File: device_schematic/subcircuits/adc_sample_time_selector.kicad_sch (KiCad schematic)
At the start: 3 parts, among them SW1 ADC speed switch

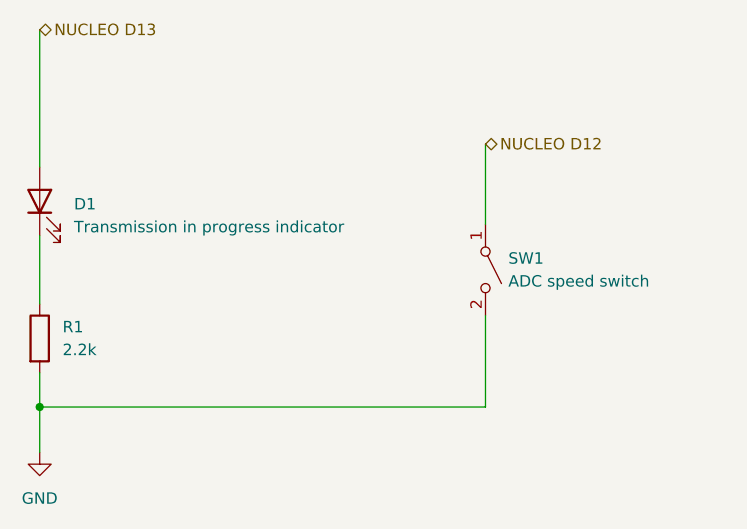
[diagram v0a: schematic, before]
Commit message: Device schematic finished version
+ correction to use D7 in place of D13
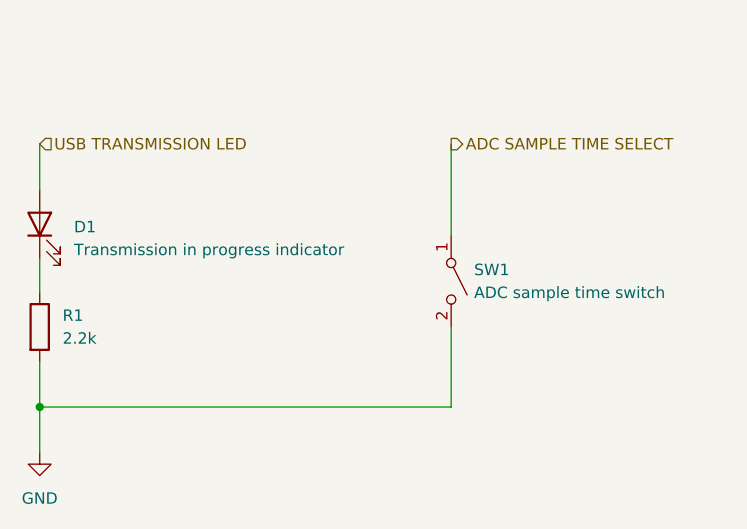
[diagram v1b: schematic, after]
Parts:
- SW1: value ADC speed switch -> ADC sample time switch
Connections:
- net NUCLEO D12 renamed ADC SAMPLE TIME SELECT
- net NUCLEO D13 renamed USB TRANSMISSION LED
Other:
- moved on the sheet: D1, R1, SW1
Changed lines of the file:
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@@
   (junction (at 110.49 119.38) (diameter 0) (color 0 0 0 0)
   )
-  (wire (pts (xy 110.49 119.38) (xy 160.02 119.38))
+  (wire (pts (xy 110.49 119.38) (xy 156.21 119.38))
     (stroke (width 0) (type default) (color 0 0 0 0))
   )
-  (wire (pts (xy 110.49 100.33) (xy 110.49 107.95))
+  (wire (pts (xy 110.49 102.87) (xy 110.49 106.68))
     (stroke (width 0) (type default) (color 0 0 0 0))
   )
-  (wire (pts (xy 160.02 90.17) (xy 160.02 99.06))
+  (wire (pts (xy 156.21 90.17) (xy 156.21 100.33))
     (stroke (width 0) (type default) (color 0 0 0 0))
   )
-  (wire (pts (xy 160.02 109.22) (xy 160.02 119.38))
+  (wire (pts (xy 156.21 110.49) (xy 156.21 119.38))
     (stroke (width 0) (type default) (color 0 0 0 0))
   )
-  (wire (pts (xy 110.49 77.47) (xy 110.49 92.71))
+  (wire (pts (xy 110.49 90.17) (xy 110.49 95.25))
     (stroke (width 0) (type default) (color 0 0 0 0))
   )
-  (wire (pts (xy 110.49 115.57) (xy 110.49 119.38))
+  (wire (pts (xy 110.49 114.3) (xy 110.49 119.38))
     (stroke (width 0) (type default) (color 0 0 0 0))
   )
@@
     (stroke (width 0) (type default) (color 0 0 0 0))
   )
-  (hierarchical_label "NUCLEO D13" (shape bidirectional) (at 110.49 77.47 0)
+  (hierarchical_label "USB TRANSMISSION LED" (shape input) (at 110.49 90.17 0)
     (effects (font (size 1.27 1.27)) (justify left))
   )
-  (hierarchical_label "NUCLEO D12" (shape bidirectional) (at 160.02 90.17 0)
+  (hierarchical_label "ADC SAMPLE TIME SELECT" (shape output) (at 156.21 90.17 0)
     (effects (font (size 1.27 1.27)) (justify left))
   )
-  (symbol (lib_id "Device:R") (at 110.49 111.76 0) (unit 1)
+  (symbol (lib_id "Device:R") (at 110.49 110.49 0) (unit 1)
     (in_bom yes) (on_board yes) (fields_autoplaced)
-    (property "Reference" "R1" (id 0) (at 113.03 110.4899 0)
+    (property "Reference" "R1" (id 0) (at 113.03 109.2199 0)
       (effects (font (size 1.27 1.27)) (justify left))
     )
-    (property "Value" "2.2k" (id 1) (at 113.03 113.0299 0)
+    (property "Value" "2.2k" (id 1) (at 113.03 111.7599 0)
       (effects (font (size 1.27 1.27)) (justify left))
     )
-    (property "Footprint" "" (id 2) (at 108.712 111.76 90)
+    (property "Footprint" "" (id 2) (at 108.712 110.49 90)
       (effects (font (size 1.27 1.27)) hide)
     )
-    (property "Datasheet" "~" (id 3) (at 110.49 111.76 0)
+    (property "Datasheet" "~" (id 3) (at 110.49 110.49 0)
       (effects (font (size 1.27 1.27)) hide)
     )
@@
     (pin "1")
   )
-  (symbol (lib_id "Device:LED") (at 110.49 96.52 90) (unit 1)
+  (symbol (lib_id "Device:LED") (at 110.49 99.06 90) (unit 1)
     (in_bom yes) (on_board yes) (fields_autoplaced)
-    (property "Reference" "D1" (id 0) (at 114.3 96.8374 90)
+    (property "Reference" "D1" (id 0) (at 114.3 99.3774 90)
       (effects (font (size 1.27 1.27)) (justify right))
     )
-    (property "Value" "Transmission in progress indicator" (id 1) (at 114.3 99.3774 90)
+    (property "Value" "Transmission in progress indicator" (id 1) (at 114.3 101.9174 90)
       (effects (font (size 1.27 1.27)) (justify right))
     )
-    (property "Footprint" "" (id 2) (at 110.49 96.52 0)
+    (property "Footprint" "" (id 2) (at 110.49 99.06 0)
       (effects (font (size 1.27 1.27)) hide)
     )
-    (property "Datasheet" "~" (id 3) (at 110.49 96.52 0)
+    (property "Datasheet" "~" (id 3) (at 110.49 99.06 0)
       (effects (font (size 1.27 1.27)) hide)
     )
@@
     (pin "2")
   )
-  (symbol (lib_id "Switch:SW_SPST") (at 160.02 104.14 270) (unit 1)
+  (symbol (lib_id "Switch:SW_SPST") (at 156.21 105.41 270) (unit 1)
     (in_bom yes) (on_board yes)
-    (property "Reference" "SW1" (id 0) (at 162.56 102.8699 90)
+    (property "Reference" "SW1" (id 0) (at 158.75 104.1399 90)
       (effects (font (size 1.27 1.27)) (justify left))
     )
-    (property "Value" "ADC speed switch" (id 1) (at 162.56 105.4099 90)
+    (property "Value" "ADC sample time switch" (id 1) (at 158.75 106.6799 90)
       (effects (font (size 1.27 1.27)) (justify left))
     )
-    (property "Footprint" "" (id 2) (at 160.02 104.14 0)
+    (property "Footprint" "" (id 2) (at 156.21 105.41 0)
       (effects (font (size 1.27 1.27)) hide)
     )
-    (property "Datasheet" "~" (id 3) (at 160.02 104.14 0)
+    (property "Datasheet" "~" (id 3) (at 156.21 105.41 0)
       (effects (font (size 1.27 1.27)) hide)
     )
